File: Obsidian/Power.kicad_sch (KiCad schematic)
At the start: 86 parts, among them J10 Barrel_Jack_Switch, J16 Conn_01x04, Q4 DMP3013SFV, U10 TPSM863257RDXR, U11 TPSM863257RDXR, U18 TLV77325PDBVR, U19 LD39100PUR, U20 RT9045AGSP / AP2303, U23 LD39100PU12RY, U24 SN74LVC1G07DBV, U25 SN74LVC1G07DBV, U4 TPSM863257RDXR, U5 TPSM863257RDXR, U6 TPSM863257RDXR

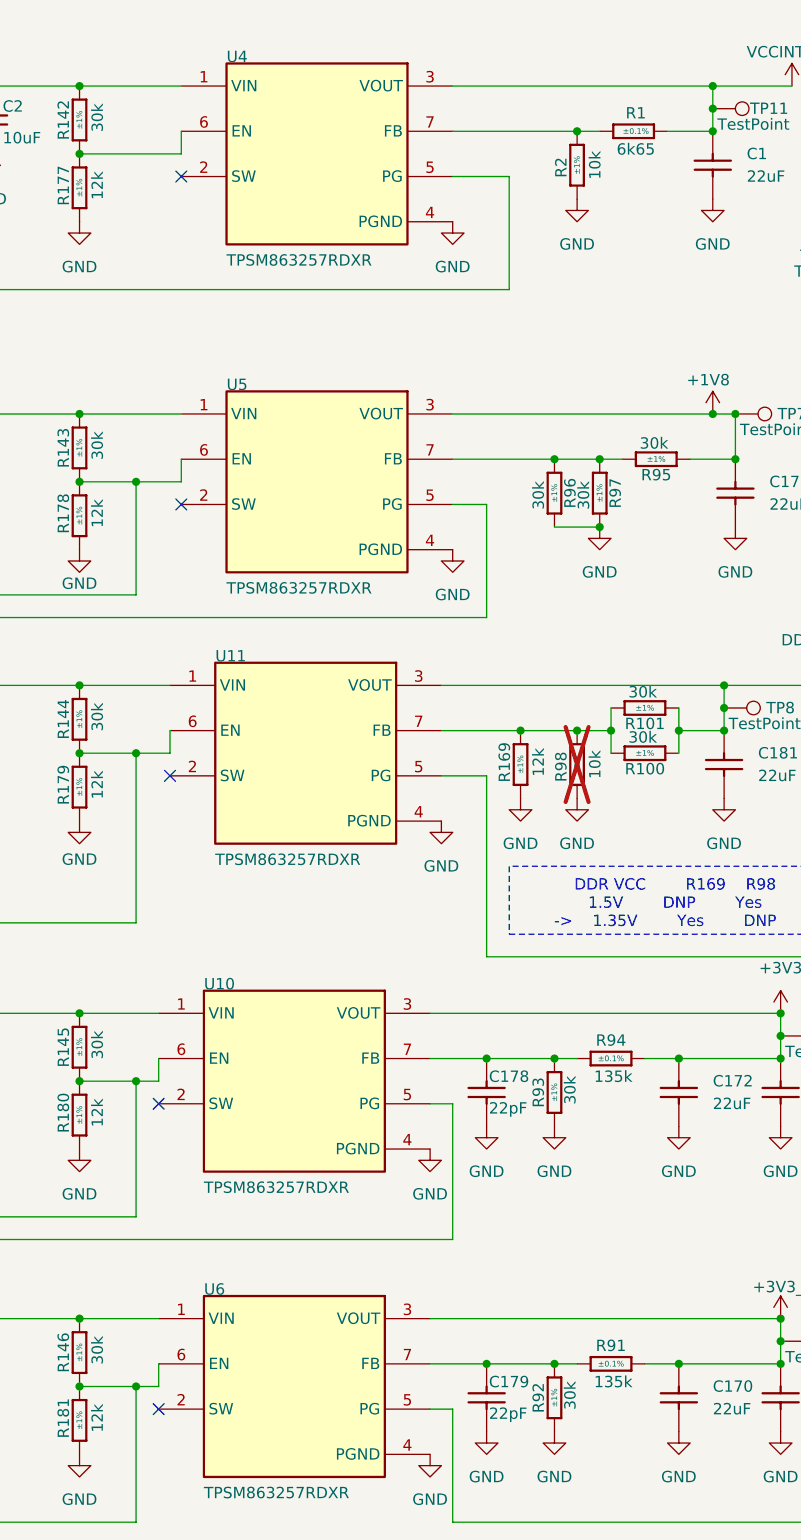
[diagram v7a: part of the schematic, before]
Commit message: Update TPSM863257RDXR symbol to set output pins as output power. Putting pull-up resistor on flash spi, decoupling capacitor and deconnect Vio.
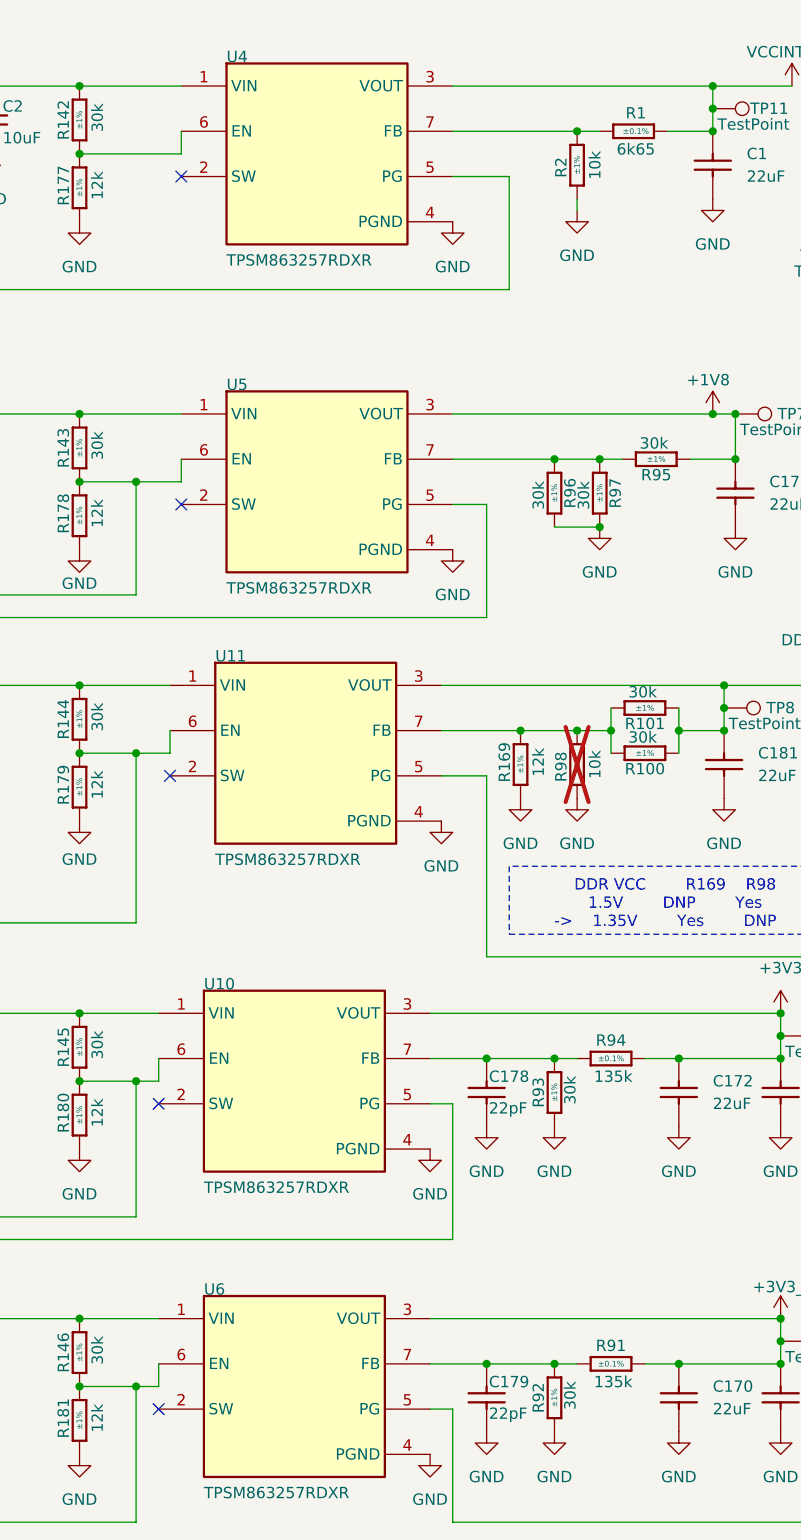
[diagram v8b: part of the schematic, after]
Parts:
- U10: symbol Library_Symbol:root_0_TPSM863257RDXR_4 -> Library_Symbol:root_0_TPSM863257RDXR_1
- U11: symbol Library_Symbol:root_0_TPSM863257RDXR_3 -> Library_Symbol:root_0_TPSM863257RDXR_1
- U5: symbol Library_Symbol:root_0_TPSM863257RDXR_2 -> Library_Symbol:root_0_TPSM863257RDXR_1
- U6: symbol Library_Symbol:root_0_TPSM863257RDXR -> Library_Symbol:root_0_TPSM863257RDXR_1
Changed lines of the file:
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@@
 	(wire
 		(pts
+			(xy 139.7 31.75) (xy 139.7 30.48)
+		)
+		(stroke
+			(width 0)
+			(type default)
+		)
+	)
+	(wire
+		(pts
 			(xy 129.54 127) (xy 137.16 127)
 		)
@@
 	(wire
 		(pts
+			(xy 125.73 17.78) (xy 154.94 17.78)
+		)
+		(stroke
+			(width 0)
+			(type default)
+		)
+	)
+	(wire
+		(pts
 			(xy 125.73 64.77) (xy 129.54 64.77)
 		)
@@
 	(wire
 		(pts
-			(xy 125.73 17.78) (xy 154.94 17.78)
-		)
-		(stroke
-			(width 0)
-			(type default)
-		)
-	)
-	(wire
-		(pts
 			(xy 208.28 81.28) (xy 208.28 82.55)
 		)
@@
 	(symbol
 		(lib_id "Library_Symbol:GND")
-		(at 139.7 30.48 0)
+		(at 139.7 31.75 0)
 		(unit 1)
 		(exclude_from_sim no)
@@
 		(fields_autoplaced yes)
 		(property "Reference" "#PWR03"
-			(at 139.7 36.83 0)
+			(at 139.7 38.1 0)
 			(effects
 				(font
@@
 		)
 		(property "Value" "GND"
-			(at 139.7 35.56 0)
+			(at 139.7 36.83 0)
 			(effects
 				(font
@@
 		)
 		(property "Footprint" ""
-			(at 139.7 30.48 0)
+			(at 139.7 31.75 0)
 			(effects
 				(font
@@
 		)
 		(property "Datasheet" ""
-			(at 139.7 30.48 0)
+			(at 139.7 31.75 0)
 			(effects
 				(font
@@
 		)
 		(property "Description" "Power symbol creates a global label with name \"GND\" , ground"
-			(at 139.7 30.48 0)
+			(at 139.7 31.75 0)
 			(effects
 				(font
@@
 	)
 	(symbol
-		(lib_name "root_0_TPSM863257RDXR_4")
-		(lib_id "Library_Symbol:root_0_TPSM863257RDXR_4")
+		(lib_id "Library_Symbol:root_0_TPSM863257RDXR_1")
 		(at 107.95 129.54 0)
 		(unit 1)
@@
 	)
 	(symbol
-		(lib_name "root_0_TPSM863257RDXR_2")
-		(lib_id "Library_Symbol:root_0_TPSM863257RDXR_2")
+		(lib_id "Library_Symbol:root_0_TPSM863257RDXR_1")
 		(at 110.49 62.23 0)
 		(unit 1)
@@
 	)
 	(symbol
-		(lib_name "root_0_TPSM863257RDXR_3")
-		(lib_id "Library_Symbol:root_0_TPSM863257RDXR_3")
+		(lib_id "Library_Symbol:root_0_TPSM863257RDXR_1")
 		(at 109.22 92.71 0)
 		(unit 1)
@@
 	)
 	(symbol
-		(lib_name "root_0_TPSM863257RDXR_1")
 		(lib_id "Library_Symbol:root_0_TPSM863257RDXR_1")
 		(at 110.49 25.4 0)
@@
 	)
 	(symbol
-		(lib_id "Library_Symbol:root_0_TPSM863257RDXR")
+		(lib_id "Library_Symbol:root_0_TPSM863257RDXR_1")
 		(at 107.95 163.83 0)
 		(unit 1)
